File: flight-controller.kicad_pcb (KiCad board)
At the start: 2 copper layers, 51 x 54 mm, 32 parts, among them J1 XT60PW-M, J2 SM04B-SRSS-TB, J3 XT60PW-F, J4 XT60PW-F, J5 XT60PW-F, J6 XT60PW-F, U1 ACS773LCB-100B-PFF, U2 LMR33630ADDA, U3 AMS1117-3.3

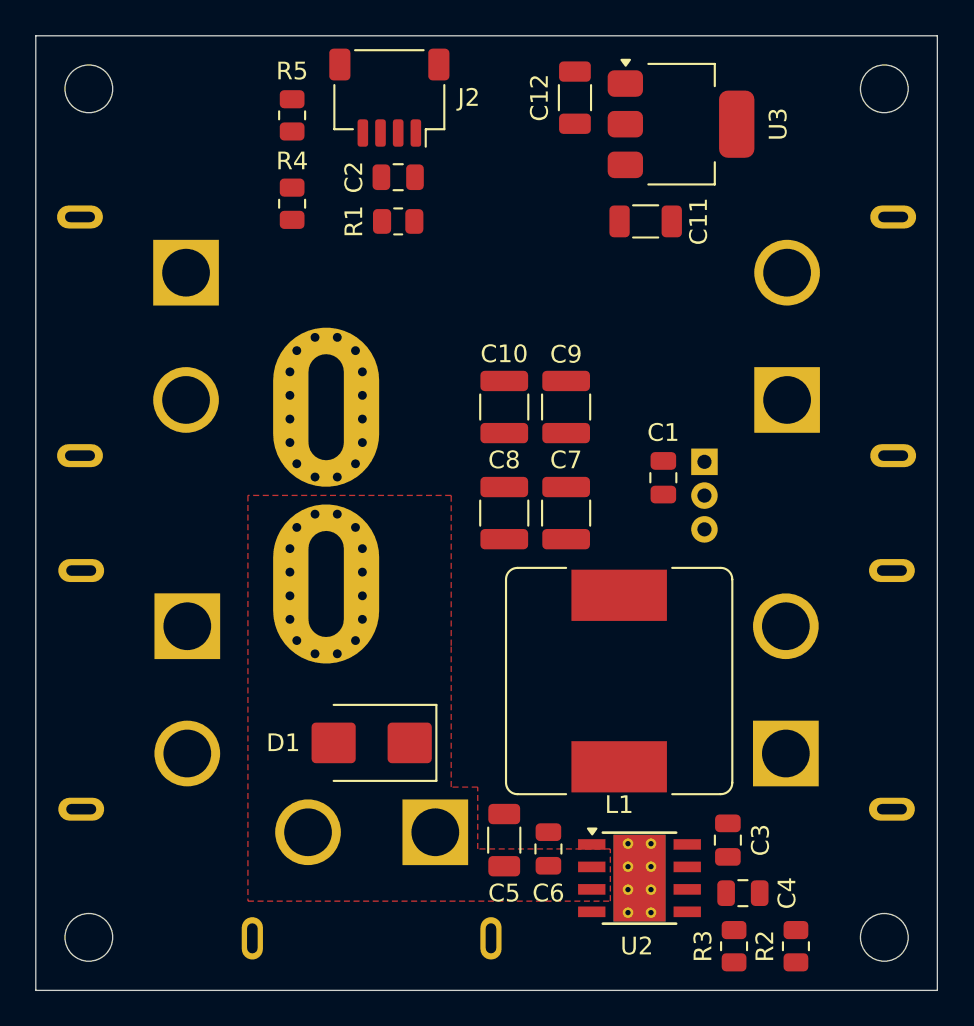
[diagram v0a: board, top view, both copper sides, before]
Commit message: feat: Added VBAT_SW plane
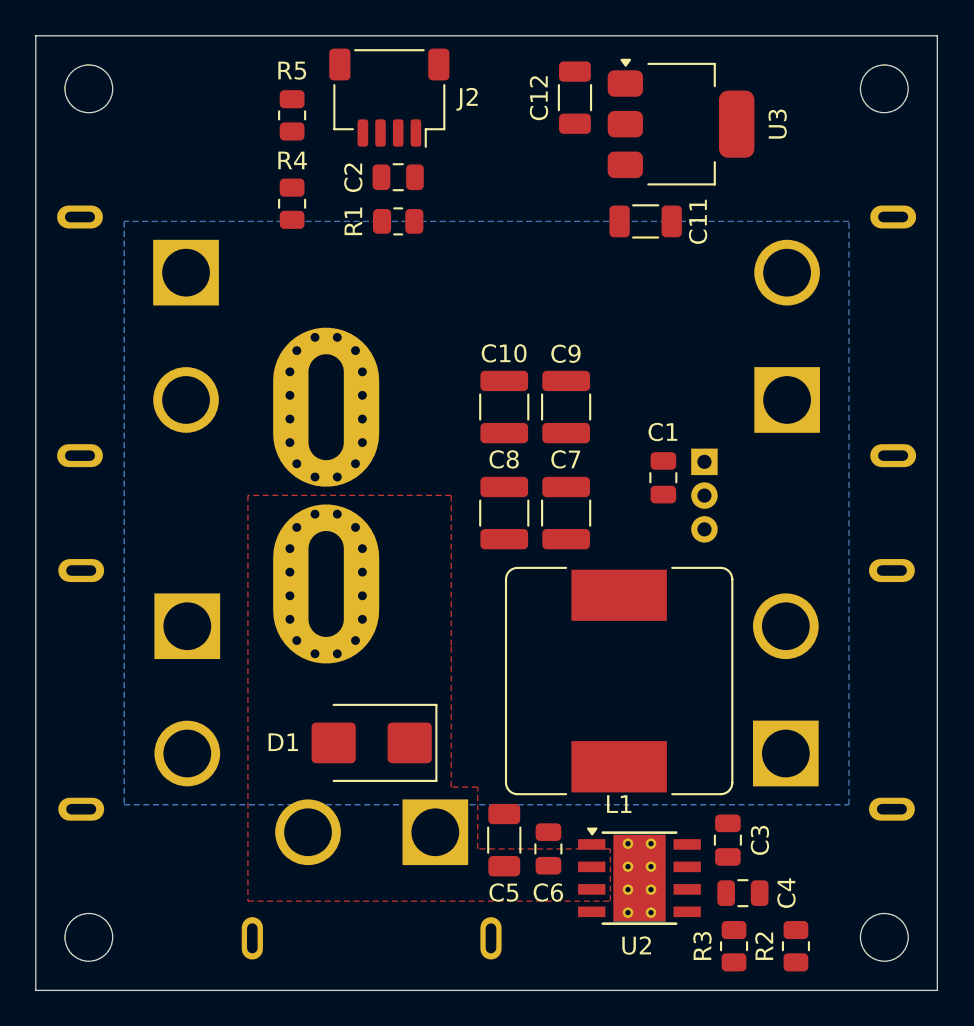
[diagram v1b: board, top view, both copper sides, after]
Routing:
- added copper zone on B.Cu, net /VBAT_SW
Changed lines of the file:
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@@
+    )
+  )
+  (zone (net 10) (net_name "/VBAT_SW") (layer "B.Cu") (hatch edge 0.5)
+    (priority 1)
+    (connect_pads yes (clearance 0.5))
+    (min_thickness 0.5) (filled_areas_thickness no)
+    (fill yes (thermal_gap 0.5) (thermal_bridge_width 0.5))
+    (polygon
+      (pts
+        (xy 119 122.5)
+        (xy 160 122.5)
+        (xy 160 89.5)
+        (xy 119 89.5)
+      )
     )
   )

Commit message: feat: Finished routing 5V
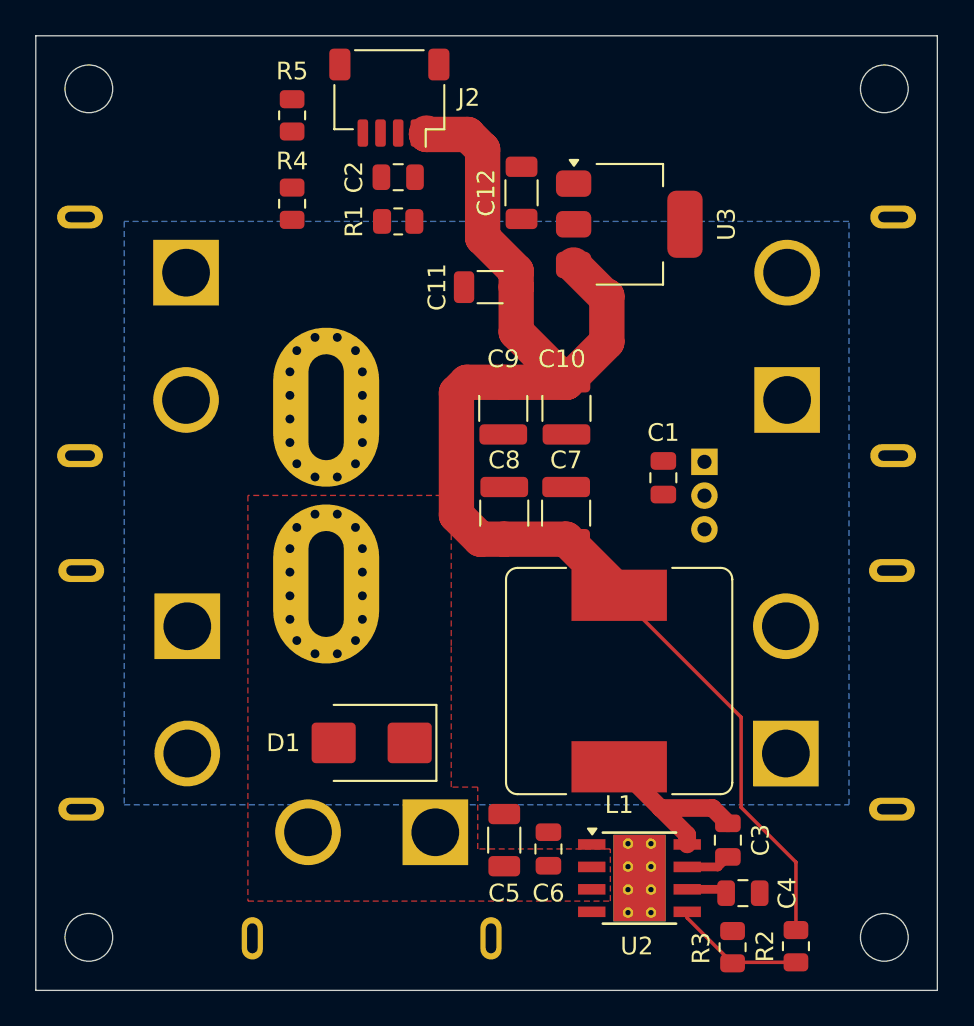
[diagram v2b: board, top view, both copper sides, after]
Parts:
- moved C11 9.55 mm to (139.7, 93.2), turned to 180 degrees
- moved U3 6.37 mm to (147.6, 89.7)
- moved C12 6.17 mm to (141.5, 87.9)
- moved C9 3.56 mm to (140.4, 100.1), turned to -90 degrees
- moved C10 3.52 mm to (144.0, 100.1), turned to -90 degrees
- moved R3 0.10 mm to (153.4, 130.6), turned to 90 degrees
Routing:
- net +5V: track 0.00 -> 74.8 mm
- net Net-(U2-SW): track 0.00 -> 10.2 mm
- net Net-(U2-FB): track 0.00 -> 7.58 mm
- net Net-(U2-BOOT): track 0.00 -> 2.53 mm
- net Net-(U2-VCC): track 0.00 -> 2.29 mm

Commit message: feat: Added 3.3V trace and VBAT_SW
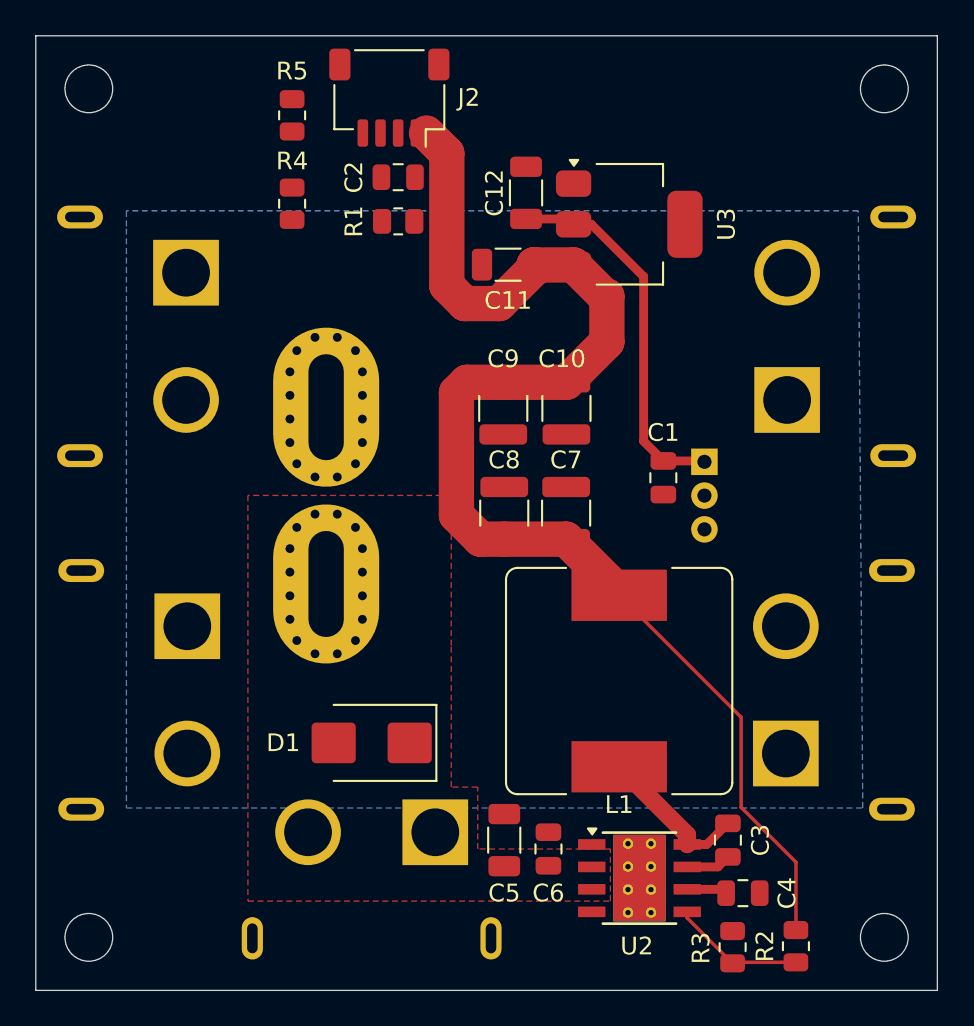
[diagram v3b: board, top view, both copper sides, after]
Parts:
- moved C11 1.63 mm to (140.7, 91.9)
- moved C12 0.25 mm to (141.7, 87.9)
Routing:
- net +3.3V: track 0.00 -> 21.2 mm
- net Net-(U2-SW): track 10.2 -> 8.78 mm
- net +5V: track 74.8 -> 73.8 mm
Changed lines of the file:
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@@
   )
   (footprint "Capacitor_SMD:C_1206_3216Metric" (layer "F.Cu")
-    (at 139.7 93.218 180)
+    (at 140.716 91.948 180)
     (descr "Capacitor SMD 1206 (3216 Metric), square (rectangular) end terminal, IPC_7351 nominal, (Body size source: IPC-SM-782 page 76, https://www.pcb-3d.com/wordpress/wp-content/uploads/ipc-sm-782a_amendment_1_and_2.pdf), generated with kicad-footprint-generator")
     (tags "capacitor")
@@
     (property "ki_keywords" "cap capacitor")
     (attr smd)
-    (fp_text reference "C11" (at 3 0 90) (layer "F.SilkS")
+    (fp_text reference "C11" (at 0 -2.032 180) (layer "F.SilkS")
         (effects (font (size 1 1) (thickness 0.15)))
     )
@@
   )
   (footprint "Capacitor_SMD:C_1206_3216Metric" (layer "F.Cu")
-    (at 141.478 87.884 90)
+    (at 141.732 87.884 90)
     (descr "Capacitor SMD 1206 (3216 Metric), square (rectangular) end terminal, IPC_7351 nominal, (Body size source: IPC-SM-782 page 76, https://www.pcb-3d.com/wordpress/wp-content/uploads/ipc-sm-782a_amendment_1_and_2.pdf), generated with kicad-footprint-generator")
     (tags "capacitor")
@@
     (property "ki_keywords" "cap capacitor")
     (attr smd)
-    (fp_text reference "C12" (at 0 -2 270) (layer "F.SilkS")
-        (effects (font (size 1 1) (thickness 0.15)))
-    )
-    (fp_text value "10uF" (at 0.024 -1.874 90) (layer "F.Fab")
+    (fp_text reference "C12" (at 0 -1.778 270) (layer "F.SilkS")
+        (effects (font (size 1 1) (thickness 0.15)))
+    )
+    (fp_text value "10uF" (at 2.794 0.254 180) (layer "F.Fab")
         (effects (font (size 1 1) (thickness 0.15)))
     )
@@
   (gr_rect (start 114 79) (end 165 133)
     (stroke (width 0.05) (type default)) (fill none) (layer "Edge.Cuts"))
+  (segment (start 144.424 89.662) (end 145.424 89.662) (width 0.5) (layer "F.Cu") (net 1))
+  (segment (start 144.121 89.359) (end 144.424 89.662) (width 0.5) (layer "F.Cu") (net 1))
+  (segment (start 141.732 89.359) (end 144.121 89.359) (width 0.5) (layer "F.Cu") (net 1))
+  (segment (start 148.385 101.935) (end 149.5 103.05) (width 0.5) (layer "F.Cu") (net 1))
+  (segment (start 151.775 103.05) (end 151.825 103.1) (width 0.5) (layer "F.Cu") (net 1))
+  (segment (start 149.5 103.05) (end 151.775 103.05) (width 0.5) (layer "F.Cu") (net 1))
+  (segment (start 145.424 89.662) (end 148.385 92.623) (width 0.5) (layer "F.Cu") (net 1))
+  (segment (start 148.385 92.623) (end 148.385 101.935) (width 0.5) (layer "F.Cu") (net 1))
   (segment (start 152.585 126.015) (end 150.85 126.015) (width 0.5) (layer "F.Cu") (net 4))
   (segment (start 153.15 125.45) (end 152.585 126.015) (width 0.5) (layer "F.Cu") (net 4))
-  (segment (start 152.282 122.682) (end 149.352 122.682) (width 1) (layer "F.Cu") (net 5))
-  (segment (start 147 120.35) (end 149.342 122.692) (width 1) (layer "F.Cu") (net 5))
-  (segment (start 150.85 124.2) (end 150.85 124.745) (width 1) (layer "F.Cu") (net 5))
-  (segment (start 153.15 123.55) (end 152.282 122.682) (width 1) (layer "F.Cu") (net 5))
-  (segment (start 149.342 122.692) (end 150.85 124.2) (width 1) (layer "F.Cu") (net 5))
-  (segment (start 149.352 122.682) (end 149.342 122.692) (width 1) (layer "F.Cu") (net 5))
+  (segment (start 150.85 124.745) (end 151.955 124.745) (width 0.5) (layer "F.Cu") (net 5))
+  (segment (start 150.85 124.2) (end 147 120.35) (width 1) (layer "F.Cu") (net 5))
+  (segment (start 150.85 124.745) (end 150.85 124.2) (width 1) (layer "F.Cu") (net 5))
+  (segment (start 151.955 124.745) (end 153.15 123.55) (width 0.5) (layer "F.Cu") (net 5))
   (segment (start 152.835 127.285) (end 153.05 127.5) (width 0.5) (layer "F.Cu") (net 6))
   (segment (start 150.85 127.285) (end 152.835 127.285) (width 0.5) (layer "F.Cu") (net 6))
+  (segment (start 144.424 91.962) (end 142.205 91.962) (width 2) (layer "F.Cu") (net 8))
   (segment (start 144.018 98.601) (end 146.304 96.315) (width 2) (layer "F.Cu") (net 8))
   (segment (start 147 110.475) (end 144 107.475) (width 2) (layer "F.Cu") (net 8))
+  (segment (start 138.267042 94.148) (end 137.25 93.130958) (width 2) (layer "F.Cu") (net 8))
   (segment (start 147 110.65) (end 153.901166 117.551166) (width 0.2) (layer "F.Cu") (net 8))
   (segment (start 144 107.475) (end 140.5 107.475) (width 2) (layer "F.Cu") (net 8))
   (segment (start 144.018 98.601) (end 140.444 98.601) (width 2) (layer "F.Cu") (net 8))
   (segment (start 153.901166 122.65) (end 157 125.748834) (width 0.2) (layer "F.Cu") (net 8))
+  (segment (start 142.205 91.962) (end 142.191 91.948) (width 2) (layer "F.Cu") (net 8))
   (segment (start 137.794 106.119) (end 137.794 99.188) (width 2) (layer "F.Cu") (net 8))
   (segment (start 146.304 93.726) (end 146.188 93.726) (width 2) (layer "F.Cu") (net 8))
-  (segment (start 139.278 85.43) (end 138.43 84.582) (width 2) (layer "F.Cu") (net 8))
   (segment (start 140.5 107.475) (end 139.15 107.475) (width 2) (layer "F.Cu") (net 8))
-  (segment (start 141.175 93.218) (end 141.175 92.318) (width 2) (layer "F.Cu") (net 8))
+  (segment (start 137.25 85.65) (end 136.1 84.5) (width 2) (layer "F.Cu") (net 8))
   (segment (start 157 125.748834) (end 157 129.5875) (width 0.2) (layer "F.Cu") (net 8))
   (segment (start 137.794 99.188) (end 138.381 98.601) (width 2) (layer "F.Cu") (net 8))
-  (segment (start 139.278 90.421) (end 139.278 85.43) (width 2) (layer "F.Cu") (net 8))
   (segment (start 147 110.65) (end 147 110.475) (width 2) (layer "F.Cu") (net 8))
+  (segment (start 137.25 93.130958) (end 137.25 85.65) (width 2) (layer "F.Cu") (net 8))
   (segment (start 138.381 98.601) (end 140.444 98.601) (width 2) (layer "F.Cu") (net 8))
   (segment (start 139.15 107.475) (end 137.794 106.119) (width 2) (layer "F.Cu") (net 8))
+  (segment (start 142.191 92.171958) (end 140.214958 94.148) (width 2) (layer "F.Cu") (net 8))
   (segment (start 146.188 93.726) (end 144.424 91.962) (width 2) (layer "F.Cu") (net 8))
   (segment (start 146.304 96.315) (end 146.304 93.726) (width 2) (layer "F.Cu") (net 8))
+  (segment (start 142.191 91.948) (end 142.191 92.171958) (width 2) (layer "F.Cu") (net 8))
   (segment (start 153.901166 117.551166) (end 153.901166 122.65) (width 0.2) (layer "F.Cu") (net 8))
-  (segment (start 141.175 95.758) (end 144.018 98.601) (width 2) (layer "F.Cu") (net 8))
-  (segment (start 141.175 93.218) (end 141.175 95.758) (width 2) (layer "F.Cu") (net 8))
-  (segment (start 138.43 84.582) (end 136.1 84.582) (width 2) (layer "F.Cu") (net 8))
-  (segment (start 141.175 92.318) (end 139.278 90.421) (width 2) (layer "F.Cu") (net 8))
-  (segment (start 136.1 84.582) (end 136.1 84.5) (width 2) (layer "F.Cu") (net 8))
+  (segment (start 140.214958 94.148) (end 138.267042 94.148) (width 2) (layer "F.Cu") (net 8))
   (segment (start 150.85 128.9025) (end 150.85 128.555) (width 0.2) (layer "F.Cu") (net 12))
   (segment (start 153.416 131.4685) (end 150.85 128.9025) (width 0.2) (layer "F.Cu") (net 12))
@@
     (polygon
       (pts
-        (xy 119 122.5)
-        (xy 160 122.5)
-        (xy 160 89.5)
-        (xy 119 89.5)
+        (xy 119.126 122.682)
+        (xy 160.782 122.682)
+        (xy 160.528 88.9)
+        (xy 119.126 88.9)
+        (xy 119.126 89.916)
       )
     )
